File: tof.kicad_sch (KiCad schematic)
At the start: 5 parts, among them J10 Conn_01x06_Socket, J11 Conn_01x06_Socket, J12 Conn_01x06_Socket

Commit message: update
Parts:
- added J13: Conn_01x02, Connector_JST:JST_XH_B2B-XH-AM_1x02_P2.50mm_Vertical, symbol Connector_Generic:Conn_01x02
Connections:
- net scl: now also J13.2 (Pin_2)
- net sda: now also J13.1 (Pin_1)
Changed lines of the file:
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@@
 	(paper "A4")
 	(junction
+		(at 111.76 66.04)
+		(diameter 0)
+		(color 0 0 0 0)
+	)
+	(junction
+		(at 111.76 63.5)
+		(diameter 0)
+		(color 0 0 0 0)
+	)
+	(junction
 		(at 101.6 60.96)
 		(diameter 0)
@@
 	(wire
 		(pts
+			(xy 111.76 63.5) (xy 139.7 63.5)
+		)
+		(stroke
+			(width 0)
+			(type default)
+		)
+	)
+	(wire
+		(pts
 			(xy 87.63 58.42) (xy 101.6 58.42)
 		)
@@
 	(wire
 		(pts
+			(xy 101.6 60.96) (xy 111.76 60.96)
+		)
+		(stroke
+			(width 0)
+			(type default)
+		)
+	)
+	(wire
+		(pts
+			(xy 64.77 55.88) (xy 68.58 55.88)
+		)
+		(stroke
+			(width 0)
+			(type default)
+		)
+	)
+	(wire
+		(pts
+			(xy 59.69 66.04) (xy 64.77 66.04)
+		)
+		(stroke
+			(width 0)
+			(type default)
+		)
+	)
+	(wire
+		(pts
+			(xy 87.63 63.5) (xy 101.6 63.5)
+		)
+		(stroke
+			(width 0)
+			(type default)
+		)
+	)
+	(wire
+		(pts
+			(xy 101.6 58.42) (xy 111.76 58.42)
+		)
+		(stroke
+			(width 0)
+			(type default)
+		)
+	)
+	(wire
+		(pts
+			(xy 85.09 71.12) (xy 87.63 71.12)
+		)
+		(stroke
+			(width 0)
+			(type default)
+		)
+	)
+	(wire
+		(pts
+			(xy 64.77 55.88) (xy 64.77 49.53)
+		)
+		(stroke
+			(width 0)
+			(type default)
+		)
+	)
+	(wire
+		(pts
+			(xy 101.6 63.5) (xy 111.76 63.5)
+		)
+		(stroke
+			(width 0)
+			(type default)
+		)
+	)
+	(wire
+		(pts
 			(xy 101.6 66.04) (xy 111.76 66.04)
 		)
@@
 	(wire
 		(pts
-			(xy 101.6 60.96) (xy 111.76 60.96)
-		)
-		(stroke
-			(width 0)
-			(type default)
-		)
-	)
-	(wire
-		(pts
-			(xy 64.77 55.88) (xy 68.58 55.88)
-		)
-		(stroke
-			(width 0)
-			(type default)
-		)
-	)
-	(wire
-		(pts
-			(xy 59.69 66.04) (xy 64.77 66.04)
-		)
-		(stroke
-			(width 0)
-			(type default)
-		)
-	)
-	(wire
-		(pts
-			(xy 87.63 63.5) (xy 101.6 63.5)
-		)
-		(stroke
-			(width 0)
-			(type default)
-		)
-	)
-	(wire
-		(pts
-			(xy 101.6 58.42) (xy 111.76 58.42)
-		)
-		(stroke
-			(width 0)
-			(type default)
-		)
-	)
-	(wire
-		(pts
-			(xy 85.09 71.12) (xy 87.63 71.12)
-		)
-		(stroke
-			(width 0)
-			(type default)
-		)
-	)
-	(wire
-		(pts
-			(xy 64.77 55.88) (xy 64.77 49.53)
-		)
-		(stroke
-			(width 0)
-			(type default)
-		)
-	)
-	(wire
-		(pts
-			(xy 101.6 63.5) (xy 111.76 63.5)
-		)
-		(stroke
-			(width 0)
-			(type default)
-		)
-	)
-	(wire
-		(pts
 			(xy 73.66 60.96) (xy 87.63 60.96)
 		)
@@
 		(pts
 			(xy 68.58 63.5) (xy 87.63 63.5)
+		)
+		(stroke
+			(width 0)
+			(type default)
+		)
+	)
+	(wire
+		(pts
+			(xy 111.76 66.04) (xy 139.7 66.04)
 		)
 		(stroke
@@
 					(unit 1)
 				)
+			)
+		)
+	)
+	(symbol
+		(lib_id "Connector_Generic:Conn_01x02")
+		(at 144.78 66.04 0)
+		(mirror x)
+		(unit 1)
+		(exclude_from_sim no)
+		(in_bom yes)
+		(on_board yes)
+		(dnp no)
+		(property "Reference" "J13"
+			(at 147.32 66.0401 0)
+			(effects
+				(font
+					(size 1.27 1.27)
+				)
+				(justify left)
+			)
+		)
+		(property "Value" "Conn_01x02"
+			(at 147.32 63.5001 0)
+			(effects
+				(font
+					(size 1.27 1.27)
+				)
+				(justify left)
+			)
+		)
+		(property "Footprint" "Connector_JST:JST_XH_B2B-XH-AM_1x02_P2.50mm_Vertical"
+			(at 144.78 66.04 0)
+			(effects
+				(font
+					(size 1.27 1.27)
+				)
+				(hide yes)
+			)
+		)
+		(property "Datasheet" "~"
+			(at 144.78 66.04 0)
+			(effects
+				(font
+					(size 1.27 1.27)
+				)
+				(hide yes)
+			)
+		)
+		(property "Description" "Generic connector, single row, 01x02, script generated (kicad-library-utils/schlib/autogen/connector/)"
+			(at 144.78 66.04 0)
+			(effects
+				(font
+					(size 1.27 1.27)
+				)
+				(hide yes)
+			)
+		)
+		(pin "1"
+		)
+		(pin "2"
+		)
+		(instances
+			(project "carte_lidar"
+				(path "/8c7c486d-228e-4b66-b6d5-0b7cf34b4d2b/c630627c-1935-4d24-8774-1650507bc0db"
+					(reference "J13")
+					(unit 1)
+				)

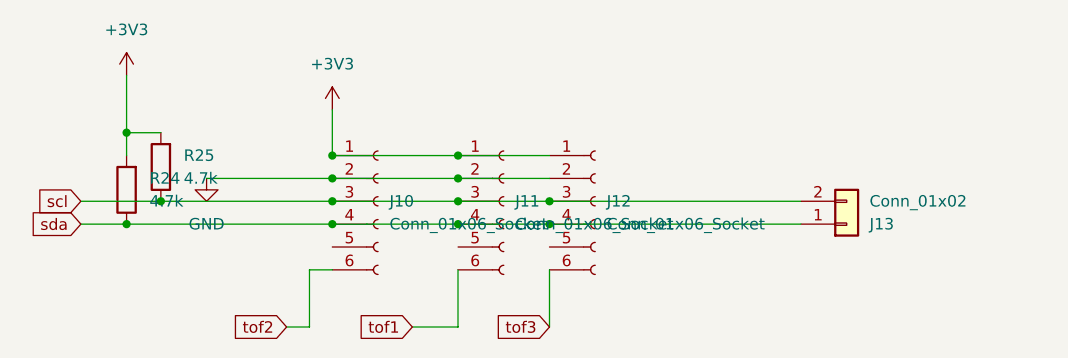
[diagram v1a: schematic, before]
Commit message: update silkscreen layer
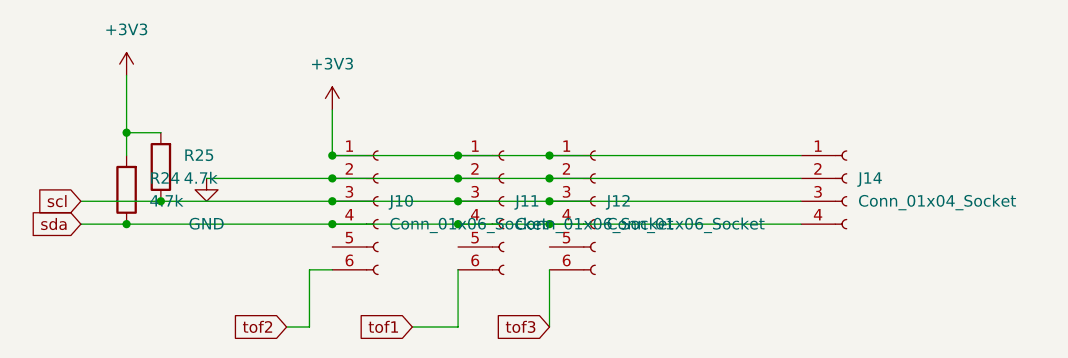
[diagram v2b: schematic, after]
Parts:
- removed J13: Conn_01x02, Connector_JST:JST_XH_B2B-XH-AM_1x02_P2.50mm_Vertical, symbol Connector_Generic:Conn_01x02
- added J14: Conn_01x04_Socket, Connector_JST:JST_XH_B4B-XH-AM_1x04_P2.50mm_Vertical, symbol Connector:Conn_01x04_Socket
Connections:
- net +3V3: now also J14.1 (Pin_1)
- net GND: now also J14.2 (Pin_2)
- net scl: now also J14.3 (Pin_3)
- net sda: now also J14.4 (Pin_4)
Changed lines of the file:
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@@
+	)
+	(junction
+		(at 111.76 60.96)
+		(diameter 0)
+		(color 0 0 0 0)
 	)
 	(junction
@@
 	)
 	(junction
+		(at 111.76 58.42)
+		(diameter 0)
+		(color 0 0 0 0)
+	)
+	(junction
 		(at 68.58 63.5)
 		(diameter 0)
@@
 	(wire
 		(pts
+			(xy 111.76 58.42) (xy 139.7 58.42)
+		)
+		(stroke
+			(width 0)
+			(type default)
+		)
+	)
+	(wire
+		(pts
 			(xy 64.77 66.04) (xy 87.63 66.04)
 		)
@@
 		(pts
 			(xy 59.69 63.5) (xy 68.58 63.5)
+		)
+		(stroke
+			(width 0)
+			(type default)
+		)
+	)
+	(wire
+		(pts
+			(xy 111.76 60.96) (xy 139.7 60.96)
 		)
 		(stroke
@@
 	)
 	(symbol
+		(lib_id "Connector:Conn_01x04_Socket")
+		(at 144.78 60.96 0)
+		(unit 1)
+		(exclude_from_sim no)
+		(in_bom yes)
+		(on_board yes)
+		(dnp no)
+		(fields_autoplaced yes)
+		(property "Reference" "J14"
+			(at 146.05 60.9599 0)
+			(effects
+				(font
+					(size 1.27 1.27)
+				)
+				(justify left)
+			)
+		)
+		(property "Value" "Conn_01x04_Socket"
+			(at 146.05 63.4999 0)
+			(effects
+				(font
+					(size 1.27 1.27)
+				)
+				(justify left)
+			)
+		)
+		(property "Footprint" "Connector_JST:JST_XH_B4B-XH-AM_1x04_P2.50mm_Vertical"
+			(at 144.78 60.96 0)
+			(effects
+				(font
+					(size 1.27 1.27)
+				)
+				(hide yes)
+			)
+		)
+		(property "Datasheet" "~"
+			(at 144.78 60.96 0)
+			(effects
+				(font
+					(size 1.27 1.27)
+				)
+				(hide yes)
+			)
+		)
+		(property "Description" "Generic connector, single row, 01x04, script generated"
+			(at 144.78 60.96 0)
+			(effects
+				(font
+					(size 1.27 1.27)
+				)
+				(hide yes)
+			)
+		)
+		(pin "1"
+		)
+		(pin "4"
+		)
+		(pin "2"
+		)
+		(pin "3"
+		)
+		(instances
+			(project "carte_lidar"
+				(path "/8c7c486d-228e-4b66-b6d5-0b7cf34b4d2b/c630627c-1935-4d24-8774-1650507bc0db"
+					(reference "J14")
+					(unit 1)
+				)
+			)
+		)
+	)
+	(symbol
 		(lib_id "power:+5V")
 		(at 87.63 53.34 0)
@@
 					(unit 1)
 				)
-			)
-		)
-	)
-	(symbol
-		(lib_id "Connector_Generic:Conn_01x02")
-		(at 144.78 66.04 0)
-		(mirror x)
-		(unit 1)
-		(exclude_from_sim no)
-		(in_bom yes)
-		(on_board yes)
-		(dnp no)
-		(property "Reference" "J13"
-			(at 147.32 66.0401 0)
-			(effects
-				(font
-					(size 1.27 1.27)
-				)
-				(justify left)
-			)
-		)
-		(property "Value" "Conn_01x02"
-			(at 147.32 63.5001 0)
-			(effects
-				(font
-					(size 1.27 1.27)
-				)
-				(justify left)
-			)
-		)
-		(property "Footprint" "Connector_JST:JST_XH_B2B-XH-AM_1x02_P2.50mm_Vertical"
-			(at 144.78 66.04 0)
-			(effects
-				(font
-					(size 1.27 1.27)
-				)
-				(hide yes)
-			)
-		)
-		(property "Datasheet" "~"
-			(at 144.78 66.04 0)
-			(effects
-				(font
-					(size 1.27 1.27)
-				)
-				(hide yes)
-			)
-		)
-		(property "Description" "Generic connector, single row, 01x02, script generated (kicad-library-utils/schlib/autogen/connector/)"
-			(at 144.78 66.04 0)
-			(effects
-				(font
-					(size 1.27 1.27)
-				)
-				(hide yes)
-			)
-		)
-		(pin "1"
-		)
-		(pin "2"
-		)
-		(instances
-			(project "carte_lidar"
-				(path "/8c7c486d-228e-4b66-b6d5-0b7cf34b4d2b/c630627c-1935-4d24-8774-1650507bc0db"
-					(reference "J13")
-					(unit 1)
-				)
